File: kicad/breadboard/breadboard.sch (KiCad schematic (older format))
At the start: 22 parts, among them J104 Conn_01x40, J105 Conn_01x40, J106 Conn_01x08, J107 Conn_01x06, J108 Conn_01x08, J49 Barrel_Jack, J64 Conn_01x40, J65 Conn_01x40, SW1 SWITCH, SW2 SWITCH, U1 AMS1117-3V3, U2 L7805, U3 ESP-12E, U4 bboard_3rows

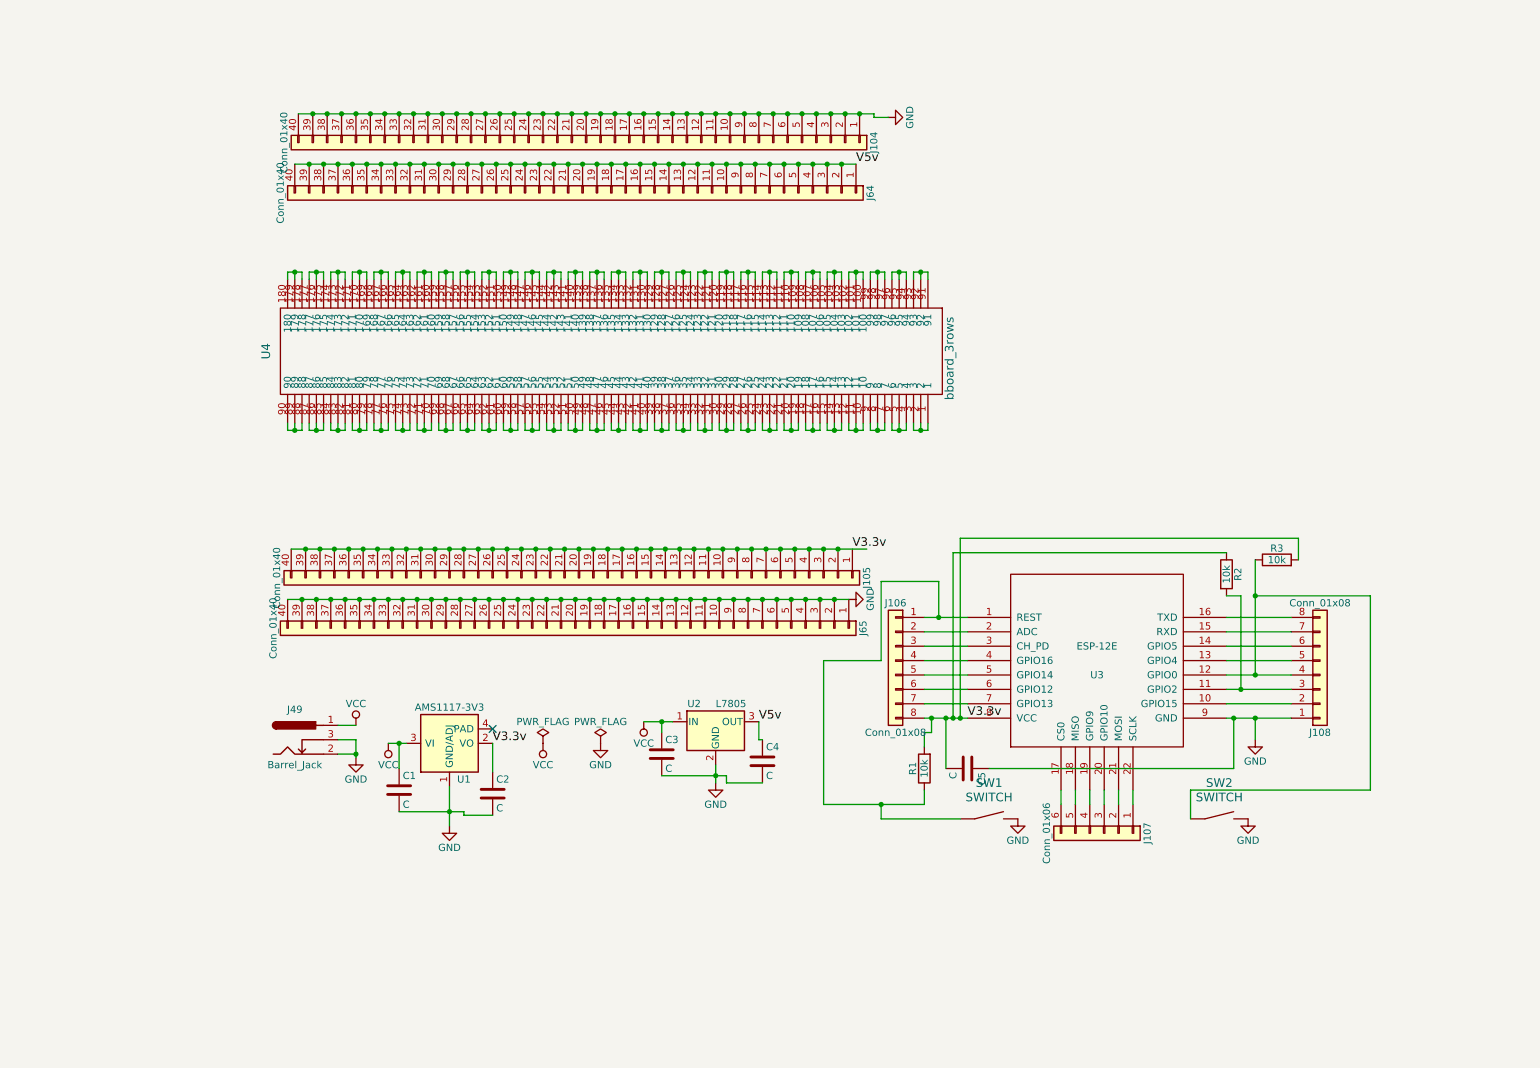
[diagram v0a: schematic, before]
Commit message: breadboard: esp12e - work is almost completed.
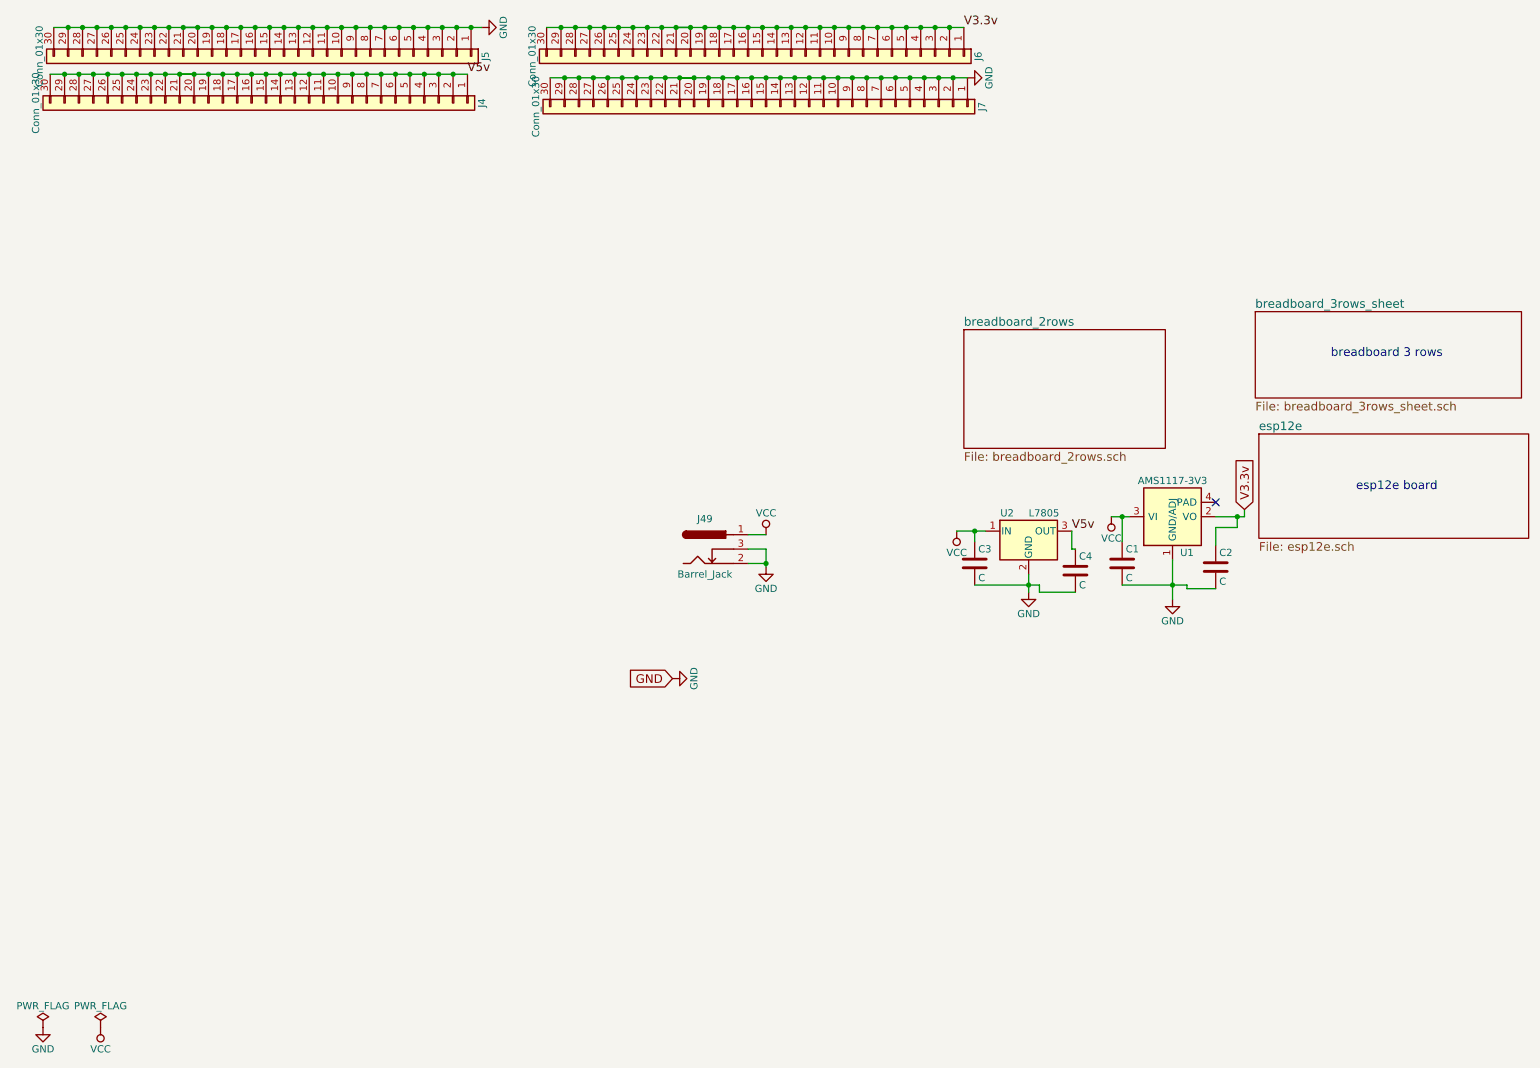
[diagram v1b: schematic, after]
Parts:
- removed C5: C, Capacitors_SMD:C_0603_HandSoldering, symbol C
- removed J104, J105, J64, J65: Conn_01x40, Pin_Headers:Pin_Header_Straight_1x40_Pitch1.27mm, symbol Conn_01x40
- removed J106, J108: Conn_01x08, Pin_Headers:Pin_Header_Straight_1x08_Pitch1.27mm, symbol Conn_01x08
- removed J107: Conn_01x06, Pin_Headers:Pin_Header_Straight_1x06_Pitch1.27mm, symbol Conn_01x06
- removed R1, R2, R3: 10k, Resistors_SMD:R_0603_HandSoldering, symbol R
- removed SW1, SW2: SWITCH, Buttons_Switches_THT:SW_PUSH_6mm, symbol SWITCH
- removed U3: ESP-12E, ESP8266:ESP-12E_SMD, symbol ESP-12E
- removed U4: bboard_3rows, symbol bboard_3rows
- added J4, J5, J6, J7: Conn_01x30, Pin_Headers:Pin_Header_Straight_1x30_Pitch2.54mm, symbol Conn_01x30
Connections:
- net GND: now also J5.1 (Pin_1), J5.10 (Pin_10), J5.11 (Pin_11), J5.12 (Pin_12), J5.13 (Pin_13), J5.14 (Pin_14), J5.15 (Pin_15), J5.16 (Pin_16), J5.17 (Pin_17), J5.18 (Pin_18), J5.19 (Pin_19), J5.2 (Pin_2), J5.20 (Pin_20), J5.21 (Pin_21), J5.22 (Pin_22), J5.23 (Pin_23), J5.24 (Pin_24), J5.25 (Pin_25), J5.26 (Pin_26), J5.27 (Pin_27), J5.28 (Pin_28), J5.29 (Pin_29), J5.3 (Pin_3), J5.30 (Pin_30), J5.4 (Pin_4), J5.5 (Pin_5), J5.6 (Pin_6), J5.7 (Pin_7), J5.8 (Pin_8), J5.9 (Pin_9), J7.1 (Pin_1), J7.10 (Pin_10), J7.11 (Pin_11), J7.12 (Pin_12), J7.13 (Pin_13), J7.14 (Pin_14), J7.15 (Pin_15), J7.16 (Pin_16), J7.17 (Pin_17), J7.18 (Pin_18), J7.19 (Pin_19), J7.2 (Pin_2), J7.20 (Pin_20), J7.21 (Pin_21), J7.22 (Pin_22), J7.23 (Pin_23), J7.24 (Pin_24), J7.25 (Pin_25), J7.26 (Pin_26), J7.27 (Pin_27), J7.28 (Pin_28), J7.29 (Pin_29), J7.3 (Pin_3), J7.30 (Pin_30), J7.4 (Pin_4), J7.5 (Pin_5), J7.6 (Pin_6), J7.7 (Pin_7), J7.8 (Pin_8), J7.9 (Pin_9)
- net V3.3v: now also J6.1 (Pin_1), J6.10 (Pin_10), J6.11 (Pin_11), J6.12 (Pin_12), J6.13 (Pin_13), J6.14 (Pin_14), J6.15 (Pin_15), J6.16 (Pin_16), J6.17 (Pin_17), J6.18 (Pin_18), J6.19 (Pin_19), J6.2 (Pin_2), J6.20 (Pin_20), J6.21 (Pin_21), J6.22 (Pin_22), J6.23 (Pin_23), J6.24 (Pin_24), J6.25 (Pin_25), J6.26 (Pin_26), J6.27 (Pin_27), J6.28 (Pin_28), J6.29 (Pin_29), J6.3 (Pin_3), J6.30 (Pin_30), J6.4 (Pin_4), J6.5 (Pin_5), J6.6 (Pin_6), J6.7 (Pin_7), J6.8 (Pin_8), J6.9 (Pin_9)
- net V5v: now also J4.1 (Pin_1), J4.10 (Pin_10), J4.11 (Pin_11), J4.12 (Pin_12), J4.13 (Pin_13), J4.14 (Pin_14), J4.15 (Pin_15), J4.16 (Pin_16), J4.17 (Pin_17), J4.18 (Pin_18), J4.19 (Pin_19), J4.2 (Pin_2), J4.20 (Pin_20), J4.21 (Pin_21), J4.22 (Pin_22), J4.23 (Pin_23), J4.24 (Pin_24), J4.25 (Pin_25), J4.26 (Pin_26), J4.27 (Pin_27), J4.28 (Pin_28), J4.29 (Pin_29), J4.3 (Pin_3), J4.30 (Pin_30), J4.4 (Pin_4), J4.5 (Pin_5), J4.6 (Pin_6), J4.7 (Pin_7), J4.8 (Pin_8), J4.9 (Pin_9)
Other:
- note added: "breadboard 3 rows\n"
- note added: "esp12e board\n"
- moved on the sheet: C1, C2, C3, C4, J49, U1, U2

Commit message: fix sch
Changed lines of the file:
@@
 $Descr A4 11693 8268
 encoding utf-8
-Sheet 1 4
+Sheet 1 3
 Title "ami's breadboard"
 Date "2017-11-12"
@@
 	0    -1   -1   0
 $EndComp
-Text Label 7125 550  0    60   ~ 0
-V3.3v
 $Comp
 L C C1
@@
 Text Notes 9850 3775 0    60   ~ 0
 esp12e board\n
-$Sheet
-S 7125 2650 1400 825
-U 5A088B98
-F0 "breadboard_2rows" 60
-F1 "breadboard_2rows.sch" 60
-$EndSheet
 $Comp
 L Conn_01x30 J5
@@
 Connection ~ 5525 550
 Wire Wire Line
-	4225 550  7125 550
+	4225 550  7275 550
 Wire Wire Line
 	5125 550  5225 550
@@
 Wire Wire Line
 	8875 4150 8875 4025
-Text GLabel 9075 3900 1    60   Input ~ 0
+Text GLabel 7275 550  2    60   Input ~ 0
 V3.3v
 Wire Wire Line
-	9075 3900 9075 3950
-Wire Wire Line
-	9075 3950 8875 3950
-Wire Wire Line
 	8875 4025 9025 4025
 Wire Wire Line
-	9025 4025 9025 3950
+	9025 4025 9025 3800
 Connection ~ 9025 3950
-Text GLabel 5100 5075 0    60   Input ~ 0
-GND
-$Comp
-L GND #PWR013
-U 1 1 5A090AC6
-P 5100 5075
-F 0 "#PWR013" H 5100 4825 50  0001 C CNN
-F 1 "GND" H 5100 4925 50  0000 C CNN
-F 2 "" H 5100 5075 50  0001 C CNN
-F 3 "" H 5100 5075 50  0001 C CNN
-	1    5100 5075
-	0    -1   -1   0
-$EndComp
+Connection ~ 7125 550
+Wire Wire Line
+	9025 3950 8875 3950
+Text GLabel 9025 3800 1    60   Input ~ 0
+V3.3v
 $EndSCHEMATC
